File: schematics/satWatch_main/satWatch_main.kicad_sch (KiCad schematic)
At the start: 117 parts, among them J1 PogoPins_02x17_Data, J2 UJ20-C-H-G-MSMT-2B-P16-TR, J5 Pogo_02x03_Power, Q1 FS8205, Q2 BSS138, Q3 DMP1045U, Q4 BSS138, SW1 B3U-1000P, SW2 B3U-1000P, SW3 B3U-1000P, SW4 B3U-1000P, SW5 B3U-1000P, U1 ESP32-S3-MINI-1, U10 VEMD8080, U11 VEMD8080, U12 BNO085, U2 MAX86141, U3 MAX32664GTGC, U4 NCP186AMX330TAG, U5 DS3231MZ, U6 MIC5365-1.8YC5, U7 PAM2401SCADJ, U8 TP4056-42-ESOP8, U9 DW01A, Y1 32.768kHz, Y2 32.768Hz

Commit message: v0.6
Began  layout work on watch-sized PCB. Backup of in-progress
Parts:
- removed C17: 22uF, Capacitor_SMD:C_0603_1608Metric_Pad1.08x0.95mm_HandSolder, symbol Device:C_Small
- removed C18, C19: 0.1uF, Capacitor_SMD:C_0603_1608Metric_Pad1.08x0.95mm_HandSolder, symbol Device:C_Small
- removed C20, C9: 10uF, Capacitor_SMD:C_0603_1608Metric_Pad1.08x0.95mm_HandSolder, symbol Device:C_Small
- removed C21, C22, C23, C5, C7: 1uF, Capacitor_SMD:C_0603_1608Metric_Pad1.08x0.95mm_HandSolder, symbol Device:C_Small
- removed D2: RED, LED_SMD:LED_0603_1608Metric_Pad1.05x0.95mm_HandSolder, symbol Device:LED
- removed D3: YELLOW, LED_SMD:LED_0603_1608Metric_Pad1.05x0.95mm_HandSolder, symbol Device:LED
- removed D6: DONE, LED_SMD:LED_0603_1608Metric_Pad1.05x0.95mm_HandSolder, symbol Device:LED
- removed D7: CHRG, LED_SMD:LED_0603_1608Metric_Pad1.05x0.95mm_HandSolder, symbol Device:LED
- removed J1: PogoPins_02x17_Data, Connector_PinHeader_2.54mm:PinHeader_2x17_P2.54mm_Vertical, symbol Connector_Generic:Conn_02x17_Counter_Clockwise
- removed J2: UJ20-C-H-G-MSMT-2B-P16-TR, footprint:SAMESKY_UJ20-C-H-G-MSMT-2B-P16-TR, symbol import_symbol:UJ20-C-H-G-MSMT-2B-P16-TR
- removed J5: Pogo_02x03_Power, Connector_PinHeader_2.54mm:PinHeader_2x03_P2.54mm_Vertical, symbol Connector_Generic:Conn_02x03_Counter_Clockwise
- removed LED1: SFH 7016, footprint:SFH7016, symbol symbols:SFH_7013
- removed Q1: FS8205, footprint:SOT95P280X145-6N, symbol symbols:FS8205
- removed R1, R29, R30, R31, R32, R33, R8: 0, Resistor_SMD:R_0603_1608Metric_Pad0.98x0.95mm_HandSolder, symbol Device:R_Small_US
- removed R10, R11: 5.1K(1%), Resistor_SMD:R_0603_1608Metric_Pad0.98x0.95mm_HandSolder, symbol Device:R_Small_US
- removed R17, R18: 22, Resistor_SMD:R_0603_1608Metric_Pad0.98x0.95mm_HandSolder, symbol Device:R_Small_US
- removed R22: 100, Resistor_SMD:R_0603_1608Metric_Pad0.98x0.95mm_HandSolder, symbol Device:R_US
- removed R23, R25, R7: 1K, Resistor_SMD:R_0603_1608Metric_Pad0.98x0.95mm_HandSolder, symbol Device:R_US
- removed R24: 1.2k, Resistor_SMD:R_0603_1608Metric_Pad0.98x0.95mm_HandSolder, symbol Device:R_US
- removed R26, R6: 10K, Resistor_SMD:R_0603_1608Metric_Pad0.98x0.95mm_HandSolder, symbol Device:R_Small_US
- removed R27: 10, Resistor_SMD:R_0603_1608Metric_Pad0.98x0.95mm_HandSolder, symbol Device:R_Small_US
- removed R28: 100K, Resistor_SMD:R_0603_1608Metric_Pad0.98x0.95mm_HandSolder, symbol Device:R_Small_US
- removed R4, R5: 5K, Resistor_SMD:R_0603_1608Metric_Pad0.98x0.95mm_HandSolder, symbol Device:R_Small_US
- removed TP10: BOOT, TestPoint:TestPoint_Pad_D2.5mm, symbol Connector:TestPoint
- removed TP11: EN, TestPoint:TestPoint_Pad_D2.5mm, symbol Connector:TestPoint
- removed TP14: BAT_MONITOR, TestPoint:TestPoint_Pad_D2.5mm, symbol Connector:TestPoint
- removed TP15: D-, TestPoint:TestPoint_Pad_D2.5mm, symbol Connector:TestPoint
- removed TP16: D+, TestPoint:TestPoint_Pad_D2.5mm, symbol Connector:TestPoint
- removed TP17: RTC_RST, TestPoint:TestPoint_Pad_D2.5mm, symbol Connector:TestPoint
- removed TP18: SQW, TestPoint:TestPoint_Pad_D2.5mm, symbol Connector:TestPoint
- removed TP19: 32KHZ, TestPoint:TestPoint_Pad_D2.5mm, symbol Connector:TestPoint
- removed TP20: BUTTON1, TestPoint:TestPoint_Pad_D2.5mm, symbol Connector:TestPoint
- removed TP21: BUTTON2, TestPoint:TestPoint_Pad_D2.5mm, symbol Connector:TestPoint
- removed TP22: BUTTON3, TestPoint:TestPoint_Pad_D2.5mm, symbol Connector:TestPoint
- removed TP23: PPG_MISO, TestPoint:TestPoint_Pad_D2.5mm, symbol Connector:TestPoint
- removed TP24: PPG_MOSI, TestPoint:TestPoint_Pad_D2.5mm, symbol Connector:TestPoint
- removed TP25: PPG_SCK, TestPoint:TestPoint_Pad_D2.5mm, symbol Connector:TestPoint
- removed TP26: PPG_CSB, TestPoint:TestPoint_Pad_D2.5mm, symbol Connector:TestPoint
- removed TP27: PPG_INT, TestPoint:TestPoint_Pad_D2.5mm, symbol Connector:TestPoint
- removed TP3: BAT+, TestPoint:TestPoint_Pad_D2.5mm, symbol Connector:TestPoint
- removed TP4: BAT-, TestPoint:TestPoint_Pad_D2.5mm, symbol Connector:TestPoint
- removed TP5: VUSB_5V, TestPoint:TestPoint_Pad_D2.5mm, symbol Connector:TestPoint
- removed TP6: VIN_3V3, TestPoint:TestPoint_Pad_D2.5mm, symbol Connector:TestPoint
- removed TP7: VCC_3V3, TestPoint:TestPoint_Pad_D2.5mm, symbol Connector:TestPoint
- removed TP8: VCC_1V8, TestPoint:TestPoint_Pad_D2.5mm, symbol Connector:TestPoint
- removed TP9: IC_5V, TestPoint:TestPoint_Pad_D2.5mm, symbol Connector:TestPoint
- removed U10, U11: VEMD8080, footprint:VEMD8080, symbol symbols:VEMD8080
- removed U2: MAX86141, footprint:MAX86141ENP, symbol symbols:MAX86141ENP+
- removed U3: MAX32664GTGC, footprint:MAX32664GTGB+T, symbol symbols:MAX32664GTGB+T
- removed U4: NCP186AMX330TAG, footprint:PSON40P160X120X45-9N, symbol import_symbol:NCP186AMX330TAG
- removed U7: PAM2401SCADJ, footprint:MSOP8_DIO, symbol import_symbol:PAM2401SCADJ
- removed U8: TP4056-42-ESOP8, Package_SO:SOIC-8-1EP_3.9x4.9mm_P1.27mm_EP2.41x3.3mm_ThermalVias, symbol Battery_Management:TP4056-42-ESOP8
- removed U9: DW01A, Package_TO_SOT_SMD:SOT-23-6, symbol Battery_Management:DW01A
- removed Y1: 32.768kHz, footprint:ABS07-32.768KHZ-T, symbol Device:Crystal
- added C13: 0.1uF, Capacitor_SMD:C_0402_1005Metric_Pad0.74x0.62mm_HandSolder, symbol Device:C_Small
- added H1, H2, H3: MountingHole, MountingHole:MountingHole_2.5mm, symbol Mechanical:MountingHole
- added J1: POGO_03x14, footprint:CUSTOM_POGO_02X21, symbol Connector_Generic:Conn_02x21_Counter_Clockwise
- added J2: Pogo_02x03_UARTPROG, footprint:CUSTOM_POGO_02X03, symbol Connector_Generic:Conn_02x03_Counter_Clockwise
- added R12: 4.7K, Resistor_SMD:R_0402_1005Metric_Pad0.72x0.64mm_HandSolder, symbol Device:R_Small_US
- added R13, R14: 0, Resistor_SMD:R_0402_1005Metric_Pad0.72x0.64mm_HandSolder, symbol Device:R_Small_US
- added U1: PAM2401SCADJ, footprint:MSOP8_DIO, symbol symbols:PAM2401SCADJ
- added U4: MAX30101EFD_T, footprint:MAX30101EFD+T, symbol symbols:MAX30101EFD_T
- C1: renamed from C11; footprint Capacitor_SMD:C_0603_1608Metric_Pad1.08x0.95mm_HandSolder -> Capacitor_SMD:C_0402_1005Metric_Pad0.74x0.62mm_HandSolder
- C10: value 0.1uF -> 10uF; footprint Capacitor_SMD:C_0603_1608Metric_Pad1.08x0.95mm_HandSolder -> Capacitor_SMD:C_0402_1005Metric_Pad0.74x0.62mm_HandSolder
- C11: renamed from C15; footprint Capacitor_SMD:C_0603_1608Metric_Pad1.08x0.95mm_HandSolder -> Capacitor_SMD:C_0402_1005Metric_Pad0.74x0.62mm_HandSolder
- C12: renamed from C13; footprint Capacitor_SMD:C_0603_1608Metric_Pad1.08x0.95mm_HandSolder -> Capacitor_SMD:C_0402_1005Metric_Pad0.74x0.62mm_HandSolder
- C14: footprint Capacitor_SMD:C_0603_1608Metric_Pad1.08x0.95mm_HandSolder -> Capacitor_SMD:C_0402_1005Metric_Pad0.74x0.62mm_HandSolder
- C15: renamed from C27; footprint Capacitor_SMD:C_0603_1608Metric_Pad1.08x0.95mm_HandSolder -> Capacitor_SMD:C_0402_1005Metric_Pad0.74x0.62mm_HandSolder
- C16: renamed from C26; footprint Capacitor_SMD:C_0603_1608Metric_Pad1.08x0.95mm_HandSolder -> Capacitor_SMD:C_0402_1005Metric_Pad0.74x0.62mm_HandSolder
- C17: renamed from C24; footprint Capacitor_SMD:C_0603_1608Metric_Pad1.08x0.95mm_HandSolder -> Capacitor_SMD:C_0402_1005Metric_Pad0.74x0.62mm_HandSolder
- C18: renamed from C25; footprint Capacitor_SMD:C_0603_1608Metric_Pad1.08x0.95mm_HandSolder -> Capacitor_SMD:C_0402_1005Metric_Pad0.74x0.62mm_HandSolder
- C2: renamed from C16; footprint Capacitor_SMD:C_0603_1608Metric_Pad1.08x0.95mm_HandSolder -> Capacitor_SMD:C_0402_1005Metric_Pad0.74x0.62mm_HandSolder
- C3: renamed from C1; footprint Capacitor_SMD:C_0603_1608Metric_Pad1.08x0.95mm_HandSolder -> Capacitor_SMD:C_0402_1005Metric_Pad0.74x0.62mm_HandSolder
- C4: renamed from C12; footprint Capacitor_SMD:C_0603_1608Metric_Pad1.08x0.95mm_HandSolder -> Capacitor_SMD:C_0402_1005Metric_Pad0.74x0.62mm_HandSolder
- C5: renamed from C8; footprint Capacitor_SMD:C_0603_1608Metric_Pad1.08x0.95mm_HandSolder -> Capacitor_SMD:C_0402_1005Metric_Pad0.74x0.62mm_HandSolder
- C6: value 1uF -> 22uF; footprint Capacitor_SMD:C_0603_1608Metric_Pad1.08x0.95mm_HandSolder -> Capacitor_SMD:C_0402_1005Metric_Pad0.74x0.62mm_HandSolder
- C7: renamed from C4; footprint Capacitor_SMD:C_0603_1608Metric_Pad1.08x0.95mm_HandSolder -> Capacitor_SMD:C_0402_1005Metric_Pad0.74x0.62mm_HandSolder
- C8: renamed from C2; footprint Capacitor_SMD:C_0603_1608Metric_Pad1.08x0.95mm_HandSolder -> Capacitor_SMD:C_0402_1005Metric_Pad0.74x0.62mm_HandSolder
- C9: renamed from C3; footprint Capacitor_SMD:C_0603_1608Metric_Pad1.08x0.95mm_HandSolder -> Capacitor_SMD:C_0402_1005Metric_Pad0.74x0.62mm_HandSolder
- D1: footprint Diode_SMD:D_0603_1608Metric_Pad1.05x0.95mm_HandSolder -> Diode_SMD:D_0402_1005Metric_Pad0.77x0.64mm_HandSolder
- L1: footprint Inductor_SMD:L_0603_1608Metric_Pad1.05x0.95mm_HandSolder -> Inductor_SMD:L_0402_1005Metric_Pad0.77x0.64mm_HandSolder
- R1: renamed from R9; footprint Resistor_SMD:R_0603_1608Metric_Pad0.98x0.95mm_HandSolder -> Resistor_SMD:R_0402_1005Metric_Pad0.72x0.64mm_HandSolder
- R10: renamed from R15; footprint Resistor_SMD:R_0603_1608Metric_Pad0.98x0.95mm_HandSolder -> Resistor_SMD:R_0402_1005Metric_Pad0.72x0.64mm_HandSolder
- R11: renamed from R20; footprint Resistor_SMD:R_0603_1608Metric_Pad0.98x0.95mm_HandSolder -> Resistor_SMD:R_0402_1005Metric_Pad0.72x0.64mm_HandSolder
- R2: renamed from R21; footprint Resistor_SMD:R_0603_1608Metric_Pad0.98x0.95mm_HandSolder -> Resistor_SMD:R_0402_1005Metric_Pad0.72x0.64mm_HandSolder
- R3: footprint Resistor_SMD:R_0603_1608Metric_Pad0.98x0.95mm_HandSolder -> Resistor_SMD:R_0402_1005Metric_Pad0.72x0.64mm_HandSolder
- R4: renamed from R12; footprint Resistor_SMD:R_0603_1608Metric_Pad0.98x0.95mm_HandSolder -> Resistor_SMD:R_0402_1005Metric_Pad0.72x0.64mm_HandSolder
- R5: renamed from R2; footprint Resistor_SMD:R_0603_1608Metric_Pad0.98x0.95mm_HandSolder -> Resistor_SMD:R_0402_1005Metric_Pad0.72x0.64mm_HandSolder
- R6: renamed from R19; footprint Resistor_SMD:R_0603_1608Metric_Pad0.98x0.95mm_HandSolder -> Resistor_SMD:R_0402_1005Metric_Pad0.72x0.64mm_HandSolder
- R7: renamed from R16; footprint Resistor_SMD:R_0603_1608Metric_Pad0.98x0.95mm_HandSolder -> Resistor_SMD:R_0402_1005Metric_Pad0.72x0.64mm_HandSolder
- R8: renamed from R14; footprint Resistor_SMD:R_0603_1608Metric_Pad0.98x0.95mm_HandSolder -> Resistor_SMD:R_0402_1005Metric_Pad0.72x0.64mm_HandSolder
- R9: renamed from R13; footprint Resistor_SMD:R_0603_1608Metric_Pad0.98x0.95mm_HandSolder -> Resistor_SMD:R_0402_1005Metric_Pad0.72x0.64mm_HandSolder
- SW3: renamed from SW5; value B3U-1000P -> EVQ-P7C01P; footprint Button_Switch_SMD:SW_SPST_B3U-1000P -> Button_Switch_SMD:SW_SPST_EVQP7C
- SW4: renamed from SW3; value B3U-1000P -> EVQ-P7C01P; footprint Button_Switch_SMD:SW_SPST_B3U-1000P -> Button_Switch_SMD:SW_SPST_EVQP7C
- SW5: renamed from SW4; value B3U-1000P -> EVQ-P7C01P; footprint Button_Switch_SMD:SW_SPST_B3U-1000P -> Button_Switch_SMD:SW_SPST_EVQP7C
- U3: renamed from U1; footprint RF_Module:ESP32-S2-MINI-1 -> footprint:ESP32-S3-MINI-1
- renumbered BT3 to BT1, Q3 to Q1, Q4 to Q3, U6 to U2, U12 to U5, U5 to U6, Y2 to Y1
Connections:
- net BAT- is gone; now on net GND: R10.2
- net USB_5V is gone; now on net 5V: C6.1
- net VCC_1V8 is gone; now on net 1V8: Q2.2 (G), Q3.2 (G), R4.1, R9.1
- net VCC_3V3 is gone; now on net 3V3: C1.1, C15.1, C2.1, C8.1, C9.1, D1.1 (K), L1.1, Q1.2, R11.1, R6.1, U2.1 (VIN), U2.3 (EN), U5.28 (VDDIO), U5.3 (VDD), U6.2 (VCC)
- net 1V8: now also C13.1, U4.11 (VDD)
- net 5V: now also C10.2, U1.7 (OUT), U4.10 (VLED+__1), U4.9 (VLED+); no longer C10.1
- net BAT+: now also Q1.3, J1.1 (Pin_1)
- net EN/CHIP_PU: now also J2.4 (Pin_4)
- net GND: now also C10.1, C13.2, J2.2 (Pin_2), U1.4 (AGND), U1.8 (PGND), U4.12 (GND), U4.4 (PGND); no longer C10.2
- net GPIO0/BOOT: now also J2.3 (Pin_3)
- net GPIO35: now also J1.11 (Pin_11)
- net GPIO36: now also J1.25 (Pin_25)
- net GPIO37: now also J1.39 (Pin_39)
- net GPIO38: now also J1.12 (Pin_12)
- net GPIO39: now also J1.26 (Pin_26)
- net GPIO40: now also J1.40 (Pin_40)
- net GPIO41: now also J1.13 (Pin_13)
- net GPIO42: now also J1.27 (Pin_27)
- net GPIO45: now also J1.41 (Pin_41)
- net GPIO46: now also J1.42 (Pin_42)
- net GPIO48: no longer U3.30 (IO48)
- net LV_SCL: now also U4.2 (SCL)
- net LV_SDA: now also U4.3 (SDA)
- net U0RXD: now also J1.28 (Pin_28), J2.5 (Pin_5), R14.2; no longer U3.40 (RXD0)
- net U0TXD: now also J1.14 (Pin_14), J2.6 (Pin_6), R13.2; no longer U3.39 (TXD0)
- net VIN_3V3: now also J2.1 (Pin_1)
- net at L1.2: now also U1.1 (LX)
- net at R2.1, R3.1: now also U1.5 (FB)
- net 32KHZ: no longer names the net of U6.1 (32KHZ)
- net ACCEL_BOOT: no longer names the net of U5.4 (~{BOOT})
- net ACCEL_CS: no longer names the net of U5.18 (~{H_CS})
- net ACCEL_INT: no longer names the net of U5.14 (~{H_INT})
- net ACCEL_MOSI: no longer names the net of U5.17 (SA0/H_MOSI)
- net ACCEL_PS0: no longer names the net of U5.6 (PS0/WAKE)
- net ACCEL_PS1: no longer names the net of U5.5 (PS1)
- net ACCEL_RST: no longer names the net of U5.11 (~{RST})
- net D+ renamed GPIO20/USBD+
- net D- renamed GPIO19/USBD-
- net ESP_3V3 renamed 3V3
- net 3V3: now also J1.2 (Pin_2), R12.2, U1.2 (EN), U1.3 (VIN)
- net GPIO1/BATTERY_MONITOR renamed GPIO1
- net GPIO1: no longer R7.1
- net RTC_RST: no longer names the net of U6.4 (~{RST})
- net SQW: no longer names the net of U6.3 (~{INT}/SQW)
- new net: R12.1, U4.13 (~{INT})
- new net: R14.1, U3.40 (RXD0)
- new net: R13.1, U3.39 (TXD0)
- new net GPIO48/BATTERY_MONITOR: R7.1, U3.30 (IO48)
- no-connect marks 11 -> 13
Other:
- note added: "I2C ADD: 0X4A"
- note added: "REFERENCE DESIGN FROM SPARKFUN MAX30101 QWIC TYPICAL CURRENT CONSUMPTION 600-1000uA VCC RANGE: 1.7 - 2.0V VCC RED/IR LED: 3.1-5.0V VCC GREN LED: 4.5-5.5V I2C ADD: 0X57"
- note added: "SWITCHES BETWEEN FRONT PANEL POWER AND PROGRAMMER-SUPPLIED POWER"
- note removed: "3.3V REGULATOR OUTPUT CURRENT: 1A QUIESCENT CURRENT: 140uA"
- note removed: "GROUND LINE ROUTES SEPERATELY FROM PHOTODIODE PAD & MAIN GROUND"
- note removed: "INTENDED FOR DOCK AND FRONTPANEL ONLY. INCLUDED WITH MAINBOARD FOR PROTOTYPING 1000mAh/1A"
- note removed: "LED1 = GREEN 530nm LED2 = IR 90nm LED3 = RED 655nm"
- note removed: "REFERENCE DESIGN FROM ANALOGDEVICES - MAXREFDES103 - SENSOR HUB REQUIRES ACCELEROMETER DATA: WILL BE FED FROM HOST-SIDE"
- moved on the sheet: BT1, C1, C11, C12, C14, C15, C16, C17, C18, C2, C3, C4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

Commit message: V0.65
mainboard progress backup
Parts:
- SW3, SW4, SW5: value EVQ-P7C01P -> EVQ-P7A01P; footprint Button_Switch_SMD:SW_SPST_EVQP7C -> Button_Switch_SMD:SW_SPST_EVQP7A
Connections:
- net EN/CHIP_PU: now also J2.1 (Pin_1); no longer J2.4 (Pin_4)
- net GND: now also J2.5 (Pin_5); no longer J2.2 (Pin_2)
- net GPIO0/BOOT: now also J2.6 (Pin_6); no longer J2.3 (Pin_3)
- net GPIO35: now also J1.39 (Pin_39); no longer J1.11 (Pin_11)
- net GPIO36: now also J1.12 (Pin_12); no longer J1.25 (Pin_25)
- net GPIO37: now also J1.26 (Pin_26); no longer J1.39 (Pin_39)
- net GPIO38: now also J1.40 (Pin_40); no longer J1.12 (Pin_12)
- net GPIO39: now also J1.13 (Pin_13); no longer J1.26 (Pin_26)
- net GPIO40: now also J1.27 (Pin_27); no longer J1.40 (Pin_40)
- net GPIO41: now also J1.41 (Pin_41); no longer J1.13 (Pin_13)
- net GPIO42: now also J1.42 (Pin_42); no longer J1.27 (Pin_27)
- net GPIO45: no longer J1.41 (Pin_41)
- net U0RXD: now also J2.2 (Pin_2); no longer J2.5 (Pin_5)
- net U0TXD: now also J2.3 (Pin_3); no longer J2.6 (Pin_6)
- net VIN_3V3: now also J2.4 (Pin_4); no longer J2.1 (Pin_1)
- net GPIO2: now reaches J1.38 (Pin_38)
- net GPIO1 renamed GPIO1/BUTTON1
- net GPIO1/BUTTON1: now also C11.1, SW3.2
- removed net GPIO2/BUTTON1: C11.1, SW3.2, U3.6 (IO2)
- net GPIO3/BUTTON2 renamed GPIO46/BUTTON2
- net GPIO46/BUTTON2: now also U3.44 (IO46); no longer U3.7 (IO3)
- removed net GPIO46: J1.42 (Pin_42), U3.44 (IO46)
- net GPIO4/BUTTON3 renamed GPIO2/BUTTON3
- net GPIO2/BUTTON3: now also U3.6 (IO2); no longer U3.8 (IO4)
- new net GPIO3: J1.25 (Pin_25), U3.7 (IO3)
- new net GPIO4: J1.11 (Pin_11), U3.8 (IO4)

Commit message: v1
Completed large prototype testing. Implementing post-fab modifications into small-form board. Finalized mainboard routing iterations and added UART programming board.
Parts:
- removed BT1: 2895 (CR1220 Holder), footprint:BAT_2895, symbol import_symbol:2895
- removed C1, C4: 1uF, Capacitor_SMD:C_0402_1005Metric_Pad0.74x0.62mm_HandSolder, symbol Device:C_Small
- removed C10, C2: 10uF, Capacitor_SMD:C_0402_1005Metric_Pad0.74x0.62mm_HandSolder, symbol Device:C_Small
- removed C11, C12, C14, C3, C5: 0.1uF/50V(10%), Capacitor_SMD:C_0402_1005Metric_Pad0.74x0.62mm_HandSolder, symbol Device:C_Small
- removed C13, C15, C16: 0.1uF, Capacitor_SMD:C_0402_1005Metric_Pad0.74x0.62mm_HandSolder, symbol Device:C_Small
- removed C17, C18: 22pF, Capacitor_SMD:C_0402_1005Metric_Pad0.74x0.62mm_HandSolder, symbol Device:C_Small
- removed C6: 22uF, Capacitor_SMD:C_0402_1005Metric_Pad0.74x0.62mm_HandSolder, symbol Device:C_Small
- removed C7, C8: 1uF/16V(10%), Capacitor_SMD:C_0402_1005Metric_Pad0.74x0.62mm_HandSolder, symbol Device:C_Small
- removed C9: 10uF/16V(10%), Capacitor_SMD:C_0402_1005Metric_Pad0.74x0.62mm_HandSolder, symbol Device:C_Small
- removed D1: SS34, Diode_SMD:D_0402_1005Metric_Pad0.77x0.64mm_HandSolder, symbol Diode:SS34
- removed H1, H2, H3: MountingHole, MountingHole:MountingHole_2.5mm, symbol Mechanical:MountingHole
- removed J1: POGO_03x14, footprint:CUSTOM_POGO_02X21, symbol Connector_Generic:Conn_02x21_Counter_Clockwise
- removed J2: Pogo_02x03_UARTPROG, footprint:CUSTOM_POGO_02X03, symbol Connector_Generic:Conn_02x03_Counter_Clockwise
- removed L1: 2.2Uh, Inductor_SMD:L_0402_1005Metric_Pad0.77x0.64mm_HandSolder, symbol Device:L_Small
- removed Q1: DMP1045U, Package_TO_SOT_SMD:SOT-23-3, symbol import_symbol:DMP1045U
- removed Q2, Q3: BSS138, Package_TO_SOT_SMD:SOT-23-3, symbol Transistor_FET_Other:Q_NMOS_Depletion_DGS
- removed R1: 10K, Resistor_SMD:R_0402_1005Metric_Pad0.72x0.64mm_HandSolder, symbol Device:R_Small_US
- removed R10, R8: 220K, Resistor_SMD:R_0402_1005Metric_Pad0.72x0.64mm_HandSolder, symbol Device:R_Small_US
- removed R11, R4, R6, R9: 2.2K, Resistor_SMD:R_0402_1005Metric_Pad0.72x0.64mm_HandSolder, symbol Device:R_Small_US
- removed R12: 4.7K, Resistor_SMD:R_0402_1005Metric_Pad0.72x0.64mm_HandSolder, symbol Device:R_Small_US
- removed R13, R14, R7: 0, Resistor_SMD:R_0402_1005Metric_Pad0.72x0.64mm_HandSolder, symbol Device:R_Small_US
- removed R2: 100K, Resistor_SMD:R_0402_1005Metric_Pad0.72x0.64mm_HandSolder, symbol Device:R_Small_US
- removed R3: 750K, Resistor_SMD:R_0402_1005Metric_Pad0.72x0.64mm_HandSolder, symbol Device:R_Small_US
- removed R5: 10K(1%), Resistor_SMD:R_0402_1005Metric_Pad0.72x0.64mm_HandSolder, symbol Device:R_Small_US
- removed SW1, SW2: B3U-1000P, Button_Switch_SMD:SW_SPST_B3U-1000P, symbol Switch:SW_Push
- removed SW3, SW4, SW5: EVQ-P7A01P, Button_Switch_SMD:SW_SPST_EVQP7A, symbol Switch:SW_Push
- removed U1: PAM2401SCADJ, footprint:MSOP8_DIO, symbol symbols:PAM2401SCADJ
- removed U2: MIC5365-1.8YC5, Package_TO_SOT_SMD:SOT-353_SC-70-5, symbol Regulator_Linear:MIC5365-1.8YC5
- removed U3: ESP32-S3-MINI-1, footprint:ESP32-S3-MINI-1, symbol RF_Module:ESP32-S3-MINI-1
- removed U4: MAX30101EFD_T, footprint:MAX30101EFD+T, symbol symbols:MAX30101EFD_T
- removed U5: BNO085, footprint:IC_BNO085, symbol symbols:BNO085
- removed U6: DS3231MZ, Package_SO:SOIC-8_3.9x4.9mm_P1.27mm, symbol Timer_RTC:DS3231MZ
- removed Y1: 32.768Hz, footprint:ABS07-32.768KHZ-T, symbol Device:Crystal
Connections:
- no-connect marks 13 -> 0
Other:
- added sheet Charger (satWatch_charger.kicad_sch)
- added sheet Mainboard (satWatch_mainboard.kicad_sch)
- added sheet Programmer (satWatch_programmer.kicad_sch)
- added sheet face1 (satWatch_face1.kicad_sch)
- note added: "DEFAULT FACEPLATE -EXTERNAL PROJECT FILE FOR FACEPLATE VARIATIONS"
- note removed: "1.8V REGULATOR OUTPUT CURRENT: 150mA QUIESCENT CURRENT: 29uA"
- note removed: "1X ON SIDE // 2X ON OTHER SIDE TYP. WAKE,SELECT,MENU / UP / DOWN"
- note removed: "DC-DC CONVERTER TO 5V FOR MAX30101 INPUT: 2.4-4.75V"
- note removed: "I2C ADD: 0X4A"
- note removed: "REFERENCE DESIGN FROM SPARKFUN MAX30101 QWIC TYPICAL CURRENT CONSUMPTION 600-1000uA VCC RANGE: 1.7 - 2.0V VCC RED/IR LED: 3.1-5.0V VCC GREN LED: 4.5-5.5V I2C ADD: 0X57"
- note removed: "SWITCHES BETWEEN FRONT PANEL POWER AND PROGRAMMER-SUPPLIED POWER"

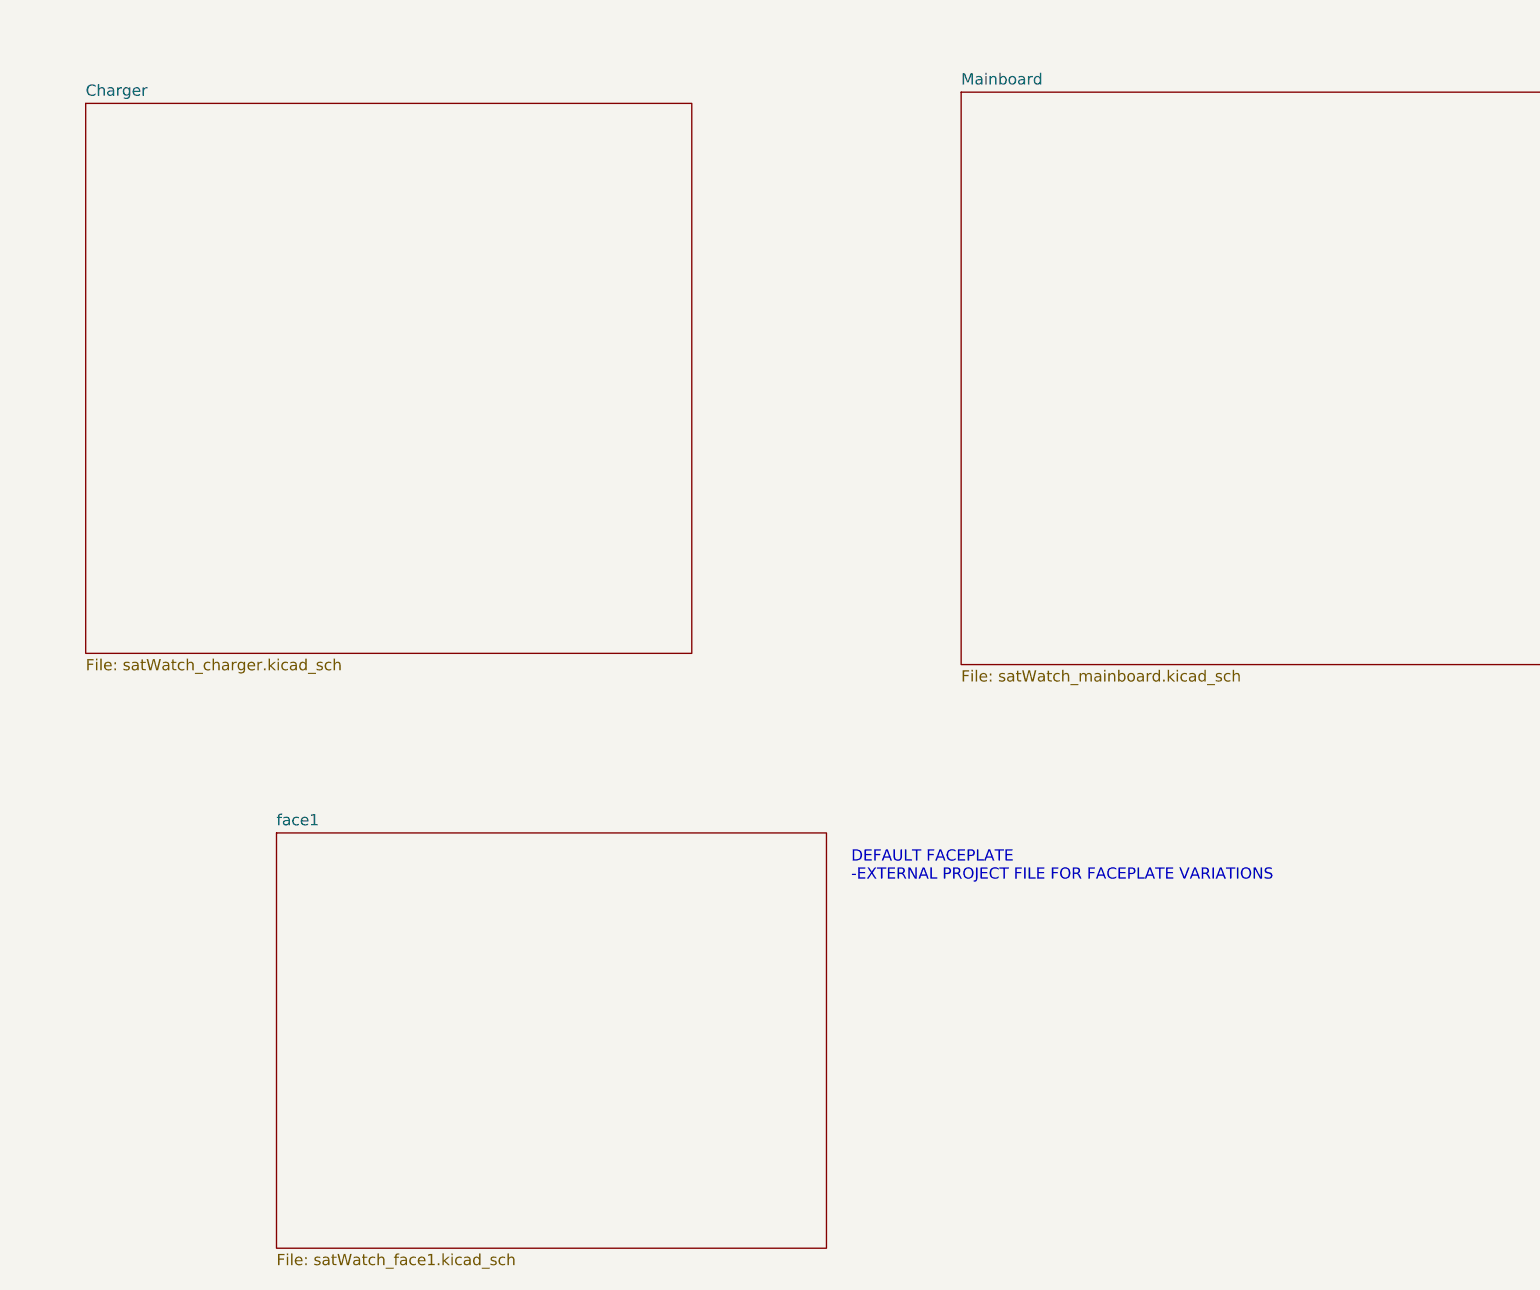
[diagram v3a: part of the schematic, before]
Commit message: v1.1
Completed board layout for charging dock configuration and a default watchface config
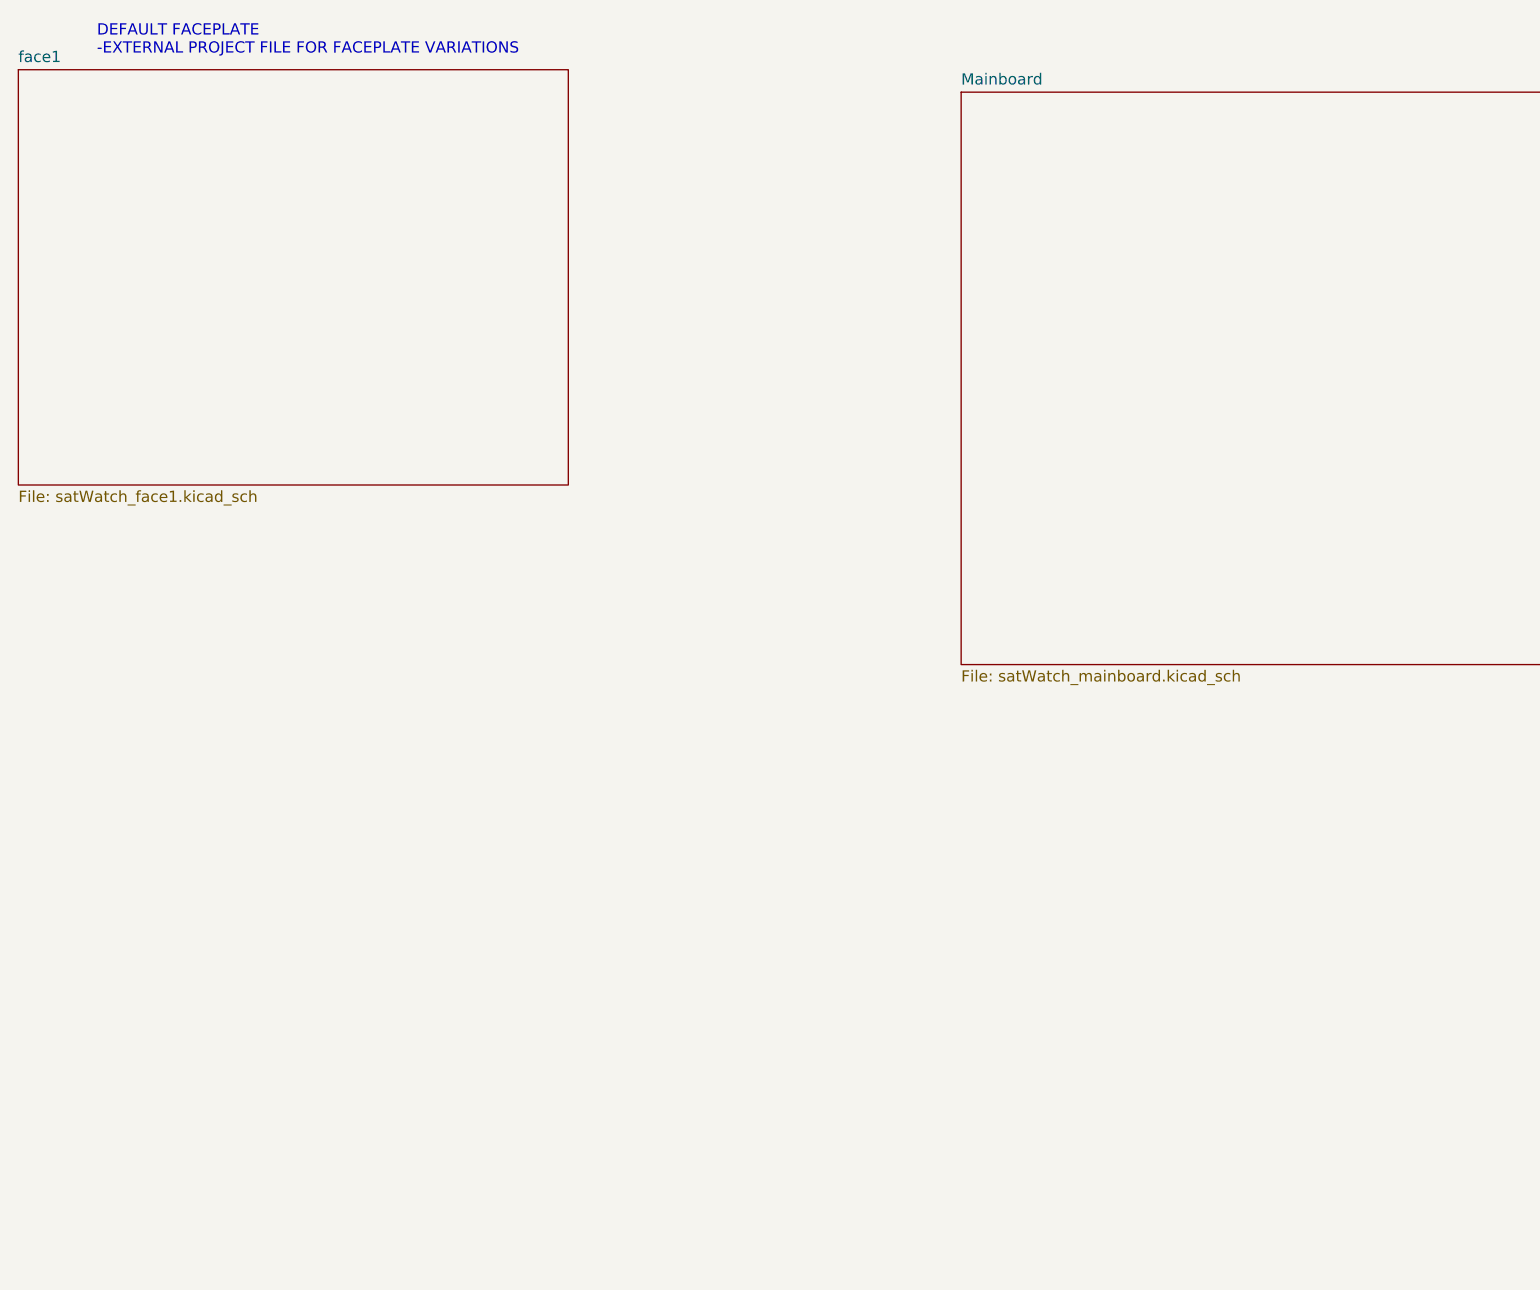
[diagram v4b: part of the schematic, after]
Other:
- removed sheet Charger
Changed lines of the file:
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@@
 	(text "DEFAULT FACEPLATE\n-EXTERNAL PROJECT FILE FOR FACEPLATE VARIATIONS\n"
 		(exclude_from_sim no)
-		(at 159.004 184.15 0)
+		(at 73.66 90.678 0)
 		(effects
 			(font
@@
 	)
 	(sheet
-		(at 93.98 180.34)
+		(at 64.77 93.98)
 		(size 62.23 46.99)
 		(exclude_from_sim no)
@@
 		)
 		(property "Sheetname" "face1"
-			(at 93.98 179.6284 0)
+			(at 64.77 93.2684 0)
 			(show_name no)
 			(do_not_autoplace no)
@@
 		)
 		(property "Sheetfile" "satWatch_face1.kicad_sch"
-			(at 93.98 227.9146 0)
+			(at 64.77 141.5546 0)
 			(show_name no)
 			(do_not_autoplace no)
@@
 				)
 			)
-		)
-	)
-	(sheet
-		(at 72.39 97.79)
-		(size 68.58 62.23)
-		(exclude_from_sim no)
-		(in_bom yes)
-		(on_board yes)
-		(dnp no)
-		(fields_autoplaced yes)
-		(stroke
-			(width 0.1524)
-			(type solid)
-		)
-		(fill
-			(color 0 0 0 0)
-		)
-		(property "Sheetname" "Charger"
-			(at 72.39 97.0784 0)
-			(show_name no)
-			(do_not_autoplace no)
-			(effects
-				(font
-					(size 1.27 1.27)
-				)
-				(justify left bottom)
-			)
-		)
-		(property "Sheetfile" "satWatch_charger.kicad_sch"
-			(at 72.39 160.6046 0)
-			(show_name no)
-			(do_not_autoplace no)
-			(effects
-				(font
-					(size 1.27 1.27)
-				)
-				(justify left top)
-			)
-		)
-		(instances
-			(project "satWatch_main"
-				(path "/b975a3df-968d-424f-9025-993d668abad1"
-					(page "4")
-				)
-			)
